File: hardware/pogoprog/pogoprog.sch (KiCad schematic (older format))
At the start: 12 parts, among them J1 USB-MINI-B, P1 CONN_6, U1 FT232RL

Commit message: added pogoprog bom info
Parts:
- C1, C3: Field1 (none) -> TDK; Field2 (none) -> C1608X7R1H104K; Field3 (none) -> Multilayer Ceramic Capacitors (MLCC) - SMD/SMT 0603 0.1uF 5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
- C2: Field1 (none) -> Kemet; Field2 (none) -> B45196H2106K109; Field3 (none) -> Tantalum Capacitors - Solid SMD 10volts 10uF 10%
- D1: Field1 (none) -> Kingbright; Field2 (none) -> APT1608SGC; Field3 (none) -> Standard LED - SMD GREEN WATER CLEAR
- D2: Field1 (none) -> Kingbright; Field2 (none) -> APT1608EC; Field3 (none) -> Standard LED - SMD HI EFF RED WTR CLR
- J1: Field1 (none) -> Kobiconn; Field2 (none) -> 154-15320-E; Field6 (none) -> USB & Firewire Connectors 5 PIN B TYPE CON RT ANGLE SMT
- R3, R4: Field1 (none) -> Bourns; Field2 (none) -> CR0603-JW-331ELF; Field3 (none) -> Thick Film Resistors - SMD 0603 330OHMS 5% 1/10WATT
- U1: Field1 (none) -> FTDI; Field2 (none) -> FT232RL; Field3 (none) -> USB Interface IC USB to Serial UART Enhanced IC SSOP-28
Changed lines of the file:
@@
-EESchema Schematic File Version 2  date Mon Dec 27 10:34:05 2010
+EESchema Schematic File Version 2  date Wed Jun  1 22:59:22 2011
 LIBS:ubertooth-symbols
 LIBS:power
@@
 LIBS:valves
 LIBS:pogoprog-cache
-EELAYER 24  0
+EELAYER 25  0
 EELAYER END
 $Descr A4 11700 8267
 Sheet 1 1
 Title "Ubertooth Pogoprog"
-Date "27 dec 2010"
+Date "2 jun 2011"
 Rev "$Rev$"
 Comp "Copyright 2010 Michael Ossmann"
@@
 F 0 "J1" H 6500 5700 60  0000 C CNN
 F 1 "USB-MINI-B" H 6500 5050 60  0000 C CNN
+F 4 "Kobiconn" H 6500 5400 60  0001 C CNN "Field1"
+F 5 "154-15320-E" H 6500 5400 60  0001 C CNN "Field2"
+F 6 "USB & Firewire Connectors 5 PIN B TYPE CON RT ANGLE SMT" H 6500 5400 60  0001 C CNN "Field6"
 	1    6500 5400
 	0    1    1    0
@@
 F 0 "C2" H 7300 4400 50  0000 L CNN
 F 1 "10μF" H 7300 4200 50  0000 L CNN
+F 4 "Kemet" H 7250 4300 60  0001 C CNN "Field1"
+F 5 "B45196H2106K109" H 7250 4300 60  0001 C CNN "Field2"
+F 6 "Tantalum Capacitors - Solid SMD 10volts 10uF 10%" H 7250 4300 60  0001 C CNN "Field3"
 	1    7250 4300
 	1    0    0    -1
@@
 F 0 "C3" H 7600 4400 50  0000 L CNN
 F 1 "100nF" H 7600 4200 50  0000 L CNN
+F 4 "TDK" H 7550 4300 60  0001 C CNN "Field1"
+F 5 "C1608X7R1H104K" H 7550 4300 60  0001 C CNN "Field2"
+F 6 "Multilayer Ceramic Capacitors (MLCC) - SMD/SMT 0603 0.1uF 50volts X7R 10%" H 7550 4300 60  0001 C CNN "Field3"
 	1    7550 4300
 	1    0    0    -1
@@
 F 0 "C1" H 6850 4700 50  0000 L CNN
 F 1 "100nF" H 6850 4500 50  0000 L CNN
+F 4 "TDK" H 6800 4600 60  0001 C CNN "Field1"
+F 5 "C1608X7R1H104K" H 6800 4600 60  0001 C CNN "Field2"
+F 6 "Multilayer Ceramic Capacitors (MLCC) - SMD/SMT 0603 0.1uF 50volts X7R 10%" H 6800 4600 60  0001 C CNN "Field3"
 	1    6800 4600
 	1    0    0    -1
@@
 F 0 "R4" V 7180 2950 50  0000 C CNN
 F 1 "330" V 7100 2950 50  0000 C CNN
+F 4 "Bourns" V 7100 2950 60  0001 C CNN "Field1"
+F 5 "CR0603-JW-331ELF" V 7100 2950 60  0001 C CNN "Field2"
+F 6 "Thick Film Resistors - SMD 0603 330OHMS 5% 1/10WATT" V 7100 2950 60  0001 C CNN "Field3"
 	1    7100 2950
 	1    0    0    -1
@@
 F 0 "R3" V 6880 2950 50  0000 C CNN
 F 1 "330" V 6800 2950 50  0000 C CNN
+F 4 "Bourns" V 6800 2950 60  0001 C CNN "Field1"
+F 5 "CR0603-JW-331ELF" V 6800 2950 60  0001 C CNN "Field2"
+F 6 "Thick Film Resistors - SMD 0603 330OHMS 5% 1/10WATT" V 6800 2950 60  0001 C CNN "Field3"
 	1    6800 2950
 	1    0    0    -1
@@
 F 0 "D2" H 7100 3600 50  0000 C CNN
 F 1 "RXLED" H 7100 3400 50  0000 C CNN
+F 4 "Kingbright" H 7100 3500 60  0001 C CNN "Field1"
+F 5 "APT1608EC" H 7100 3500 60  0001 C CNN "Field2"
+F 6 "Standard LED - SMD HI EFF RED WTR CLR" H 7100 3500 60  0001 C CNN "Field3"
 	1    7100 3500
 	0    1    1    0
@@
 F 0 "D1" H 6800 3600 50  0000 C CNN
 F 1 "TXLED" H 6800 3400 50  0000 C CNN
+F 4 "Kingbright" H 6800 3500 60  0001 C CNN "Field1"
+F 5 "APT1608SGC" H 6800 3500 60  0001 C CNN "Field2"
+F 6 "Standard LED - SMD GREEN WATER CLEAR" H 6800 3500 60  0001 C CNN "Field3"
 	1    6800 3500
 	0    1    1    0
@@
 F 0 "U1" H 5750 4600 60  0000 C CNN
 F 1 "FT232RL" H 5750 3100 60  0000 C CNN
+F 4 "FTDI" H 5750 3850 60  0001 C CNN "Field1"
+F 5 "FT232RL" H 5750 3850 60  0001 C CNN "Field2"
+F 6 "USB Interface IC USB to Serial UART Enhanced IC SSOP-28" H 5750 3850 60  0001 C CNN "Field3"
 	1    5750 3850
 	1    0    0    -1

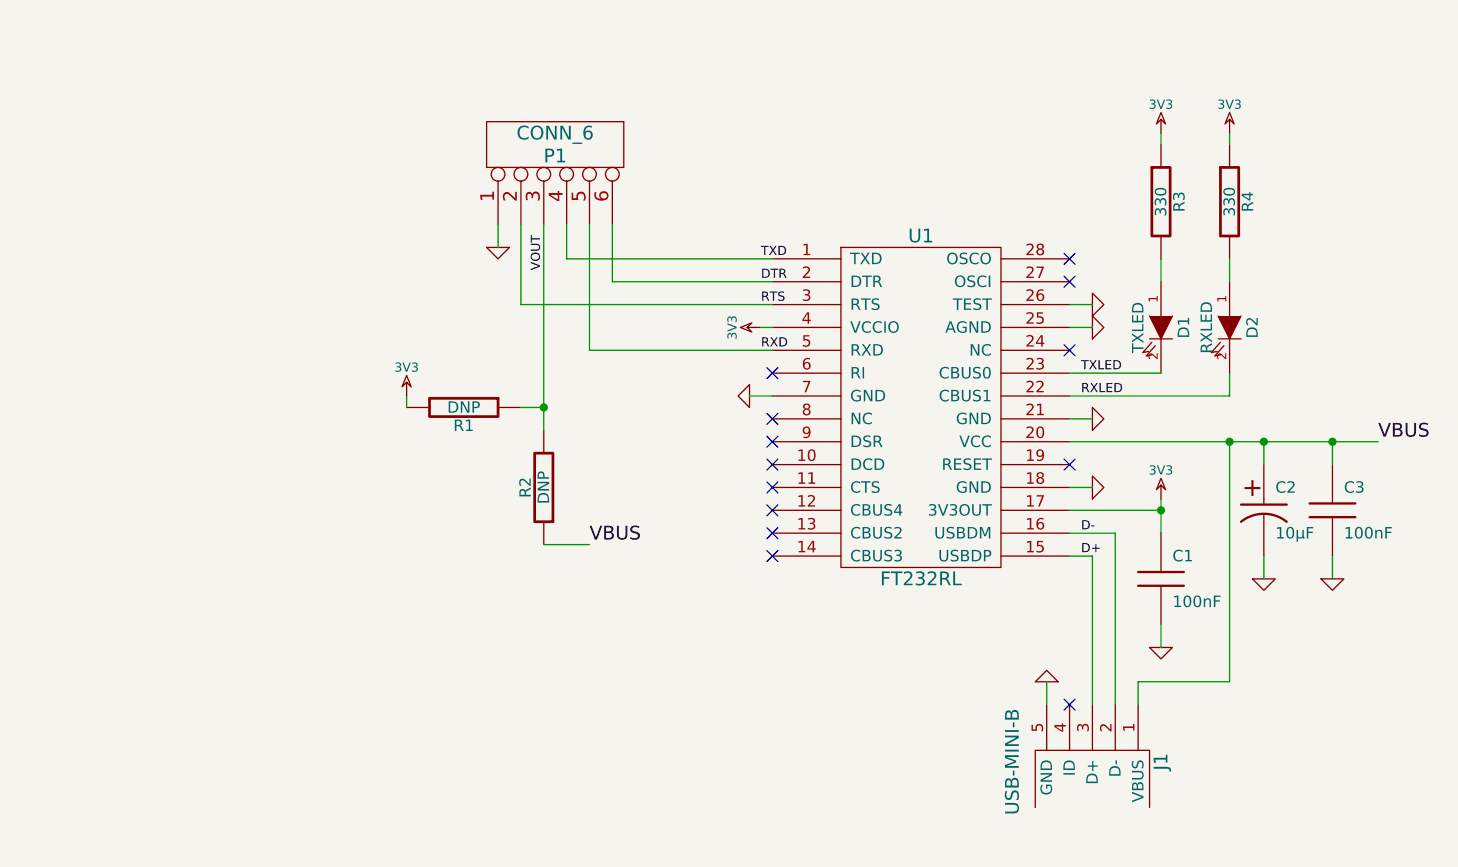
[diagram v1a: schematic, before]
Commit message: updated pogoprog: micro USB, extra header, 3V3 default output/logic, optional CTS, round edges
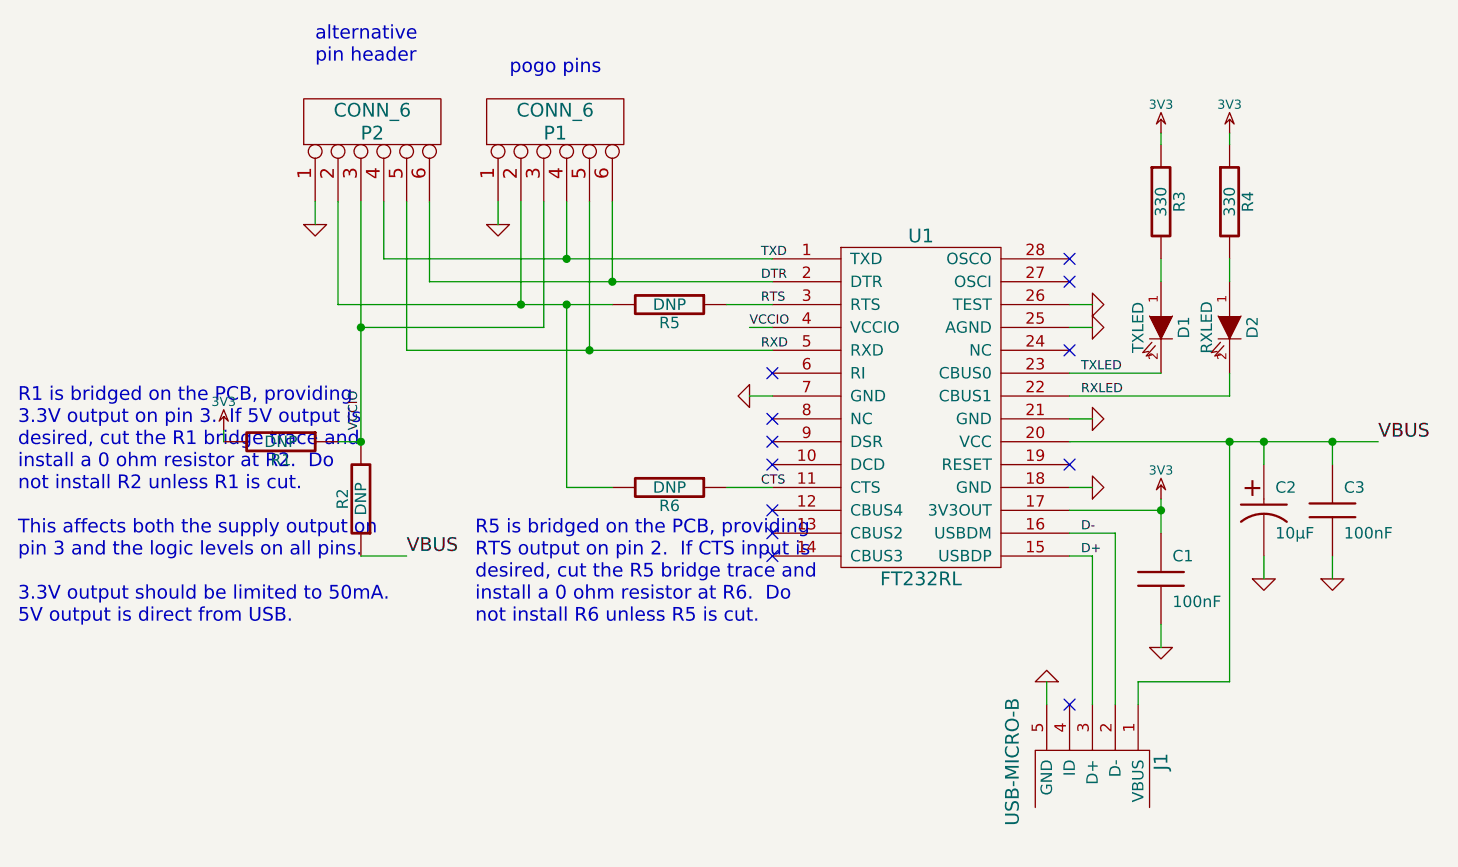
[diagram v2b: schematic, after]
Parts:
- added P2: CONN_6, symbol CONN_6
- added R5, R6: DNP, symbol R
- J1: value USB-MINI-B -> USB-MICRO-B
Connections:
- net 3V3: no longer U1.4 (VCCIO)
- net DTR: now also P2.6
- net GND: now also P2.1
- net RTS: now also R5.1; no longer P1.2
- net RXD: now also P2.5
- net TXD: now also P2.4
- net CTS: now reaches U1.11 (CTS)
- net CTS: now also R6.1
- net VOUT renamed VCCIO
- net VCCIO: now also U1.4 (VCCIO), P2.3
- new net: P1.2, P2.2, R5.2, R6.2
- no-connect marks 13 -> 12
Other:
- note added: "R1 is bridged on the PCB, providing\n3.3V output on pin 3. If 5V output is\ndesired, cut the R1 bridge trace and\ninstall a 0 ohm resistor at R2. Do\nnot install R2 unless R1 is cut.\n\nThis affects both the supply output on\npin 3 and the logic levels on all pins.\n\n3.3V output should be limited to 50mA.\n5V output is direct from USB."
- note added: "R5 is bridged on the PCB, providing\nRTS output on pin 2. If CTS input is\ndesired, cut the R5 bridge trace and\ninstall a 0 ohm resistor at R6. Do\nnot install R6 unless R5 is cut."
- note added: "alternative\npin header"
- note added: "pogo pins"
- moved on the sheet: P1, R1, R2
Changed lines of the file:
@@
-EESchema Schematic File Version 2  date Wed Jun  1 22:59:22 2011
+EESchema Schematic File Version 2  date Mon 24 Oct 2011 12:37:25 AM MDT
 LIBS:ubertooth-symbols
 LIBS:power
@@
 EELAYER END
 $Descr A4 11700 8267
+encoding utf-8
 Sheet 1 1
 Title "Ubertooth Pogoprog"
-Date "2 jun 2011"
+Date "24 oct 2011"
 Rev "$Rev$"
 Comp "Copyright 2010 Michael Ossmann"
@@
 Comment4 ""
 $EndDescr
-Wire Wire Line
-	5100 3400 4000 3400
-Wire Wire Line
-	4000 3400 4000 3050
+Text Label 5000 3500 0    40   ~ 0
+VCCIO
+Text Notes 3800 4800 0    60   ~ 0
+R5 is bridged on the PCB, providing\nRTS output on pin 2.  If CTS input is\ndesired, cut the R5 bridge trace and\ninstall a 0 ohm resistor at R6.  Do\nnot install R6 unless R5 is cut.
+Text Label 5050 4200 0    40   ~ 0
+CTS
+Text Label 5050 3400 0    40   ~ 0
+RTS
+Connection ~ 4200 3400
+Wire Wire Line
+	4200 3400 4200 4200
+Wire Wire Line
+	4200 4200 4400 4200
+Wire Wire Line
+	4900 3400 5100 3400
+Connection ~ 3300 3500
+Wire Wire Line
+	3300 2950 3300 4000
+Wire Wire Line
+	3100 3050 3100 2950
+Connection ~ 4200 3200
+Wire Wire Line
+	3400 2950 3400 3200
+Wire Wire Line
+	3400 3200 5100 3200
+Connection ~ 4400 3300
+Wire Wire Line
+	3600 2950 3600 3300
+Wire Wire Line
+	3600 3300 5100 3300
+Wire Wire Line
+	4000 2950 4000 3400
 Connection ~ 7550 4000
 Wire Wire Line
@@
 	6500 4500 6500 5150
 Wire Wire Line
-	3500 3800 3500 3850
-Wire Wire Line
-	4000 3850 4100 3850
-Wire Wire Line
-	3900 3050 3900 3150
-Wire Wire Line
-	5100 3600 4300 3600
-Wire Wire Line
-	4300 3600 4300 3050
-Wire Wire Line
-	5050 3500 5100 3500
+	2700 3950 2700 4000
+Wire Wire Line
+	3300 4000 3200 4000
+Wire Wire Line
+	3900 2950 3900 3050
+Wire Wire Line
+	4300 2950 4300 3600
+Wire Wire Line
+	5000 3500 5100 3500
 Wire Wire Line
 	6400 4200 6500 4200
@@
 	5000 3800 5100 3800
 Wire Wire Line
-	4200 3050 4200 3200
-Wire Wire Line
-	4200 3200 5100 3200
+	4200 2950 4200 3200
 Wire Wire Line
 	7750 4000 6400 4000
-Wire Wire Line
-	4100 3050 4100 3950
-Connection ~ 4100 3850
-Wire Wire Line
-	4100 4450 4300 4450
+Connection ~ 3300 4000
+Wire Wire Line
+	3300 4500 3500 4500
 Wire Wire Line
 	6600 5150 6600 4400
@@
 	6600 4400 6400 4400
 Wire Wire Line
-	6800 4300 6400 4300
+	6400 4300 6800 4300
 Wire Wire Line
 	6300 5050 6300 5150
@@
 	7250 4500 7250 4600
 Wire Wire Line
-	7250 4100 7250 4000
+	7250 4000 7250 4100
 Connection ~ 7250 4000
 Wire Wire Line
-	4400 3050 4400 3300
-Wire Wire Line
-	4400 3300 5100 3300
-Text Label 4100 3250 1    40   ~ 0
-VOUT
+	4400 2950 4400 3300
+Wire Wire Line
+	5100 3600 3500 3600
+Wire Wire Line
+	3500 3600 3500 2950
+Connection ~ 4300 3600
+Wire Wire Line
+	3200 2950 3200 3400
+Connection ~ 4000 3400
+Wire Wire Line
+	3300 3500 4100 3500
+Wire Wire Line
+	4100 3500 4100 2950
+Wire Wire Line
+	3200 3400 4400 3400
+Wire Wire Line
+	5100 4200 4900 4200
+$Comp
+L R R6
+U 1 1 4EA4EC65
+P 4650 4200
+F 0 "R6" V 4730 4200 50  0000 C CNN
+F 1 "DNP" V 4650 4200 50  0000 C CNN
+	1    4650 4200
+	0    1    1    0
+$EndComp
+$Comp
+L R R5
+U 1 1 4EA4EC49
+P 4650 3400
+F 0 "R5" V 4730 3400 50  0000 C CNN
+F 1 "DNP" V 4650 3400 50  0000 C CNN
+	1    4650 3400
+	0    1    1    0
+$EndComp
+Text Notes 1800 4800 0    60   ~ 0
+R1 is bridged on the PCB, providing\n3.3V output on pin 3.  If 5V output is\ndesired, cut the R1 bridge trace and\ninstall a 0 ohm resistor at R2.  Do\nnot install R2 unless R1 is cut.\n\nThis affects both the supply output on\npin 3 and the logic levels on all pins.\n\n3.3V output should be limited to 50mA.\n5V output is direct from USB.
+Text Notes 3100 2350 0    60   ~ 0
+alternative\npin header
+Text Notes 3950 2400 0    60   ~ 0
+pogo pins
+$Comp
+L GND #PWR01
+U 1 1 4EA4E16B
+P 3100 3050
+F 0 "#PWR01" H 3100 3050 30  0001 C CNN
+F 1 "GND" H 3100 2980 30  0001 C CNN
+	1    3100 3050
+	1    0    0    -1
+$EndComp
+Text Label 3300 3950 1    40   ~ 0
+VCCIO
+$Comp
+L CONN_6 P2
+U 1 1 4EA4E0D6
+P 3350 2600
+F 0 "P2" V 3300 2600 60  0000 C CNN
+F 1 "CONN_6" V 3400 2600 60  0000 C CNN
+	1    3350 2600
+	0    -1   -1   0
+$EndComp
 Text Label 6450 4500 0    40   ~ 0
 D+
@@
 Text Label 5050 3600 0    40   ~ 0
 RXD
-Text Label 5050 3400 0    40   ~ 0
-RTS
 Text Label 5050 3300 0    40   ~ 0
 DTR
@@
 P 6500 5400
 F 0 "J1" H 6500 5700 60  0000 C CNN
-F 1 "USB-MINI-B" H 6500 5050 60  0000 C CNN
+F 1 "USB-MICRO-B" H 6500 5050 60  0000 C CNN
 F 4 "Kobiconn" H 6500 5400 60  0001 C CNN "Field1"
 F 5 "154-15320-E" H 6500 5400 60  0001 C CNN "Field2"
@@
 $EndComp
 $Comp
-L GND #PWR01
+L GND #PWR02
 U 1 1 4CDDB287
 P 7550 4600
-F 0 "#PWR01" H 7550 4600 30  0001 C CNN
+F 0 "#PWR02" H 7550 4600 30  0001 C CNN
 F 1 "GND" H 7550 4530 30  0001 C CNN
 	1    7550 4600
@@
 $EndComp
 $Comp
-L GND #PWR02
+L GND #PWR03
 U 1 1 4CDDB285
 P 7250 4600
-F 0 "#PWR02" H 7250 4600 30  0001 C CNN
+F 0 "#PWR03" H 7250 4600 30  0001 C CNN
 F 1 "GND" H 7250 4530 30  0001 C CNN
 	1    7250 4600
@@
 $EndComp
 $Comp
-L GND #PWR03
+L GND #PWR04
 U 1 1 4CDDB238
 P 6300 5050
-F 0 "#PWR03" H 6300 5050 30  0001 C CNN
+F 0 "#PWR04" H 6300 5050 30  0001 C CNN
 F 1 "GND" H 6300 4980 30  0001 C CNN
 	1    6300 5050
@@
 	1    0    0    -1
 $EndComp
-Text Label 4300 4450 0    60   ~ 0
+Text Label 3500 4500 0    60   ~ 0
 VBUS
 $Comp
-L 3V3 #PWR04
+L 3V3 #PWR05
 U 1 1 4CDDB137
-P 3500 3800
-F 0 "#PWR04" H 3500 3900 40  0001 C CNN
-F 1 "3V3" H 3500 3925 40  0000 C CNN
-	1    3500 3800
+P 2700 3950
+F 0 "#PWR05" H 2700 4050 40  0001 C CNN
+F 1 "3V3" H 2700 4075 40  0000 C CNN
+	1    2700 3950
 	1    0    0    -1
 $EndComp
@@
 L R R2
 U 1 1 4CDDB10B
-P 4100 4200
-F 0 "R2" V 4180 4200 50  0000 C CNN
-F 1 "DNP" V 4100 4200 50  0000 C CNN
-	1    4100 4200
+P 3300 4250
+F 0 "R2" V 3380 4250 50  0000 C CNN
+F 1 "DNP" V 3300 4250 50  0000 C CNN
+	1    3300 4250
 	-1   0    0    1
 $EndComp
@@
 L R R1
 U 1 1 4CDDB0FC
-P 3750 3850
-F 0 "R1" V 3830 3850 50  0000 C CNN
-F 1 "DNP" V 3750 3850 50  0000 C CNN
-	1    3750 3850
+P 2950 4000
+F 0 "R1" V 3030 4000 50  0000 C CNN
+F 1 "DNP" V 2950 4000 50  0000 C CNN
+	1    2950 4000
 	0    1    1    0
 $EndComp
@@
 VBUS
 $Comp
-L GND #PWR05
+L GND #PWR06
 U 1 1 4CDDB090
-P 3900 3150
-F 0 "#PWR05" H 3900 3150 30  0001 C CNN
-F 1 "GND" H 3900 3080 30  0001 C CNN
-	1    3900 3150
+P 3900 3050
+F 0 "#PWR06" H 3900 3050 30  0001 C CNN
+F 1 "GND" H 3900 2980 30  0001 C CNN
+	1    3900 3050
 	1    0    0    -1
 $EndComp
@@
 L CONN_6 P1
 U 1 1 4CDDAFDF
-P 4150 2700
-F 0 "P1" V 4100 2700 60  0000 C CNN
-F 1 "CONN_6" V 4200 2700 60  0000 C CNN
-	1    4150 2700
+P 4150 2600
+F 0 "P1" V 4100 2600 60  0000 C CNN
+F 1 "CONN_6" V 4200 2600 60  0000 C CNN
+	1    4150 2600
 	0    -1   -1   0
 $EndComp
 $Comp
-L GND #PWR06
+L GND #PWR07
 U 1 1 4CDDA9D5
 P 5000 3800
-F 0 "#PWR06" H 5000 3800 30  0001 C CNN
+F 0 "#PWR07" H 5000 3800 30  0001 C CNN
 F 1 "GND" H 5000 3730 30  0001 C CNN
 	1    5000 3800
@@
 NoConn ~ 5100 4400
 NoConn ~ 5100 4300
-NoConn ~ 5100 4200
 NoConn ~ 5100 4100
 NoConn ~ 5100 4000
@@
 NoConn ~ 5100 3900
 $Comp
-L GND #PWR07
+L GND #PWR08
 U 1 1 4CDDA830
 P 6800 4900
-F 0 "#PWR07" H 6800 4900 30  0001 C CNN
+F 0 "#PWR08" H 6800 4900 30  0001 C CNN
 F 1 "GND" H 6800 4830 30  0001 C CNN
 	1    6800 4900
@@
 $EndComp
 $Comp
-L 3V3 #PWR08
-U 1 1 4CDDA753
-P 5050 3500
-F 0 "#PWR08" H 5050 3600 40  0001 C CNN
-F 1 "3V3" H 5050 3625 40  0000 C CNN
-	1    5050 3500
-	0    -1   -1   0
-$EndComp
-$Comp

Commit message: pogoprog bom corrections
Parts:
- J1: Field1 Kobiconn -> FCI; Field2 154-15320-E -> 10103594-0001LF; Field6 USB & Firewire Connectors 5 PIN B TYPE CON RT ANGLE SMT -> USB Connectors 5P Quick Connect Micro USB TypeB Rcpt
- P1: value CONN_6 -> pogopins; Field1 (none) -> SparkFun; Field2 (none) -> PRT-09174; Field3 (none) -> QTY 6 Pogo Pins w/ Pointed Tip
- P2: value CONN_6 -> DNP
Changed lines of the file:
@@
-EESchema Schematic File Version 2  date Mon 24 Oct 2011 12:37:25 AM MDT
+EESchema Schematic File Version 2  date Mon 19 Dec 2011 10:01:30 AM MST
 LIBS:ubertooth-symbols
 LIBS:power
@@
 Sheet 1 1
 Title "Ubertooth Pogoprog"
-Date "24 oct 2011"
+Date "19 dec 2011"
 Rev "$Rev$"
 Comp "Copyright 2010 Michael Ossmann"
@@
 P 3350 2600
 F 0 "P2" V 3300 2600 60  0000 C CNN
-F 1 "CONN_6" V 3400 2600 60  0000 C CNN
+F 1 "DNP" V 3400 2600 60  0000 C CNN
 	1    3350 2600
 	0    -1   -1   0
@@
 F 0 "J1" H 6500 5700 60  0000 C CNN
 F 1 "USB-MICRO-B" H 6500 5050 60  0000 C CNN
-F 4 "Kobiconn" H 6500 5400 60  0001 C CNN "Field1"
-F 5 "154-15320-E" H 6500 5400 60  0001 C CNN "Field2"
-F 6 "USB & Firewire Connectors 5 PIN B TYPE CON RT ANGLE SMT" H 6500 5400 60  0001 C CNN "Field6"
+F 4 "FCI" H 6500 5400 60  0001 C CNN "Field1"
+F 5 "10103594-0001LF" H 6500 5400 60  0001 C CNN "Field2"
+F 6 "USB Connectors 5P Quick Connect Micro USB TypeB Rcpt" H 6500 5400 60  0001 C CNN "Field6"
 	1    6500 5400
 	0    1    1    0
@@
 P 4150 2600
 F 0 "P1" V 4100 2600 60  0000 C CNN
-F 1 "CONN_6" V 4200 2600 60  0000 C CNN
+F 1 "pogopins" V 4200 2600 60  0000 C CNN
+F 4 "SparkFun" V 4150 2600 60  0001 C CNN "Field1"
+F 5 "PRT-09174" V 4150 2600 60  0001 C CNN "Field2"
+F 6 "QTY 6 Pogo Pins w/ Pointed Tip" V 4150 2600 60  0001 C CNN "Field3"
 	1    4150 2600
 	0    -1   -1   0
